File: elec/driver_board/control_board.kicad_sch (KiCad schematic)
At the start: 20 parts, among them J1 rotary_encoder, J2 DCF77 board, J3 RTC, U1 ESP32-C3-DEVKITM-1, U2 TXB0102DCT

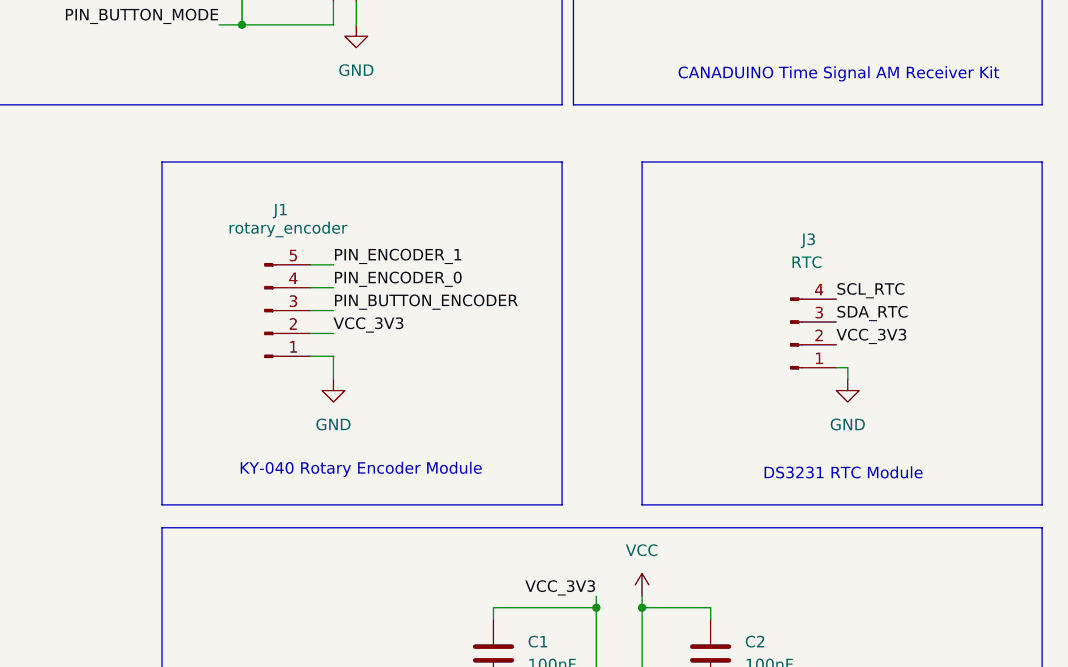
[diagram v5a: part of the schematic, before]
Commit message: Update hole size
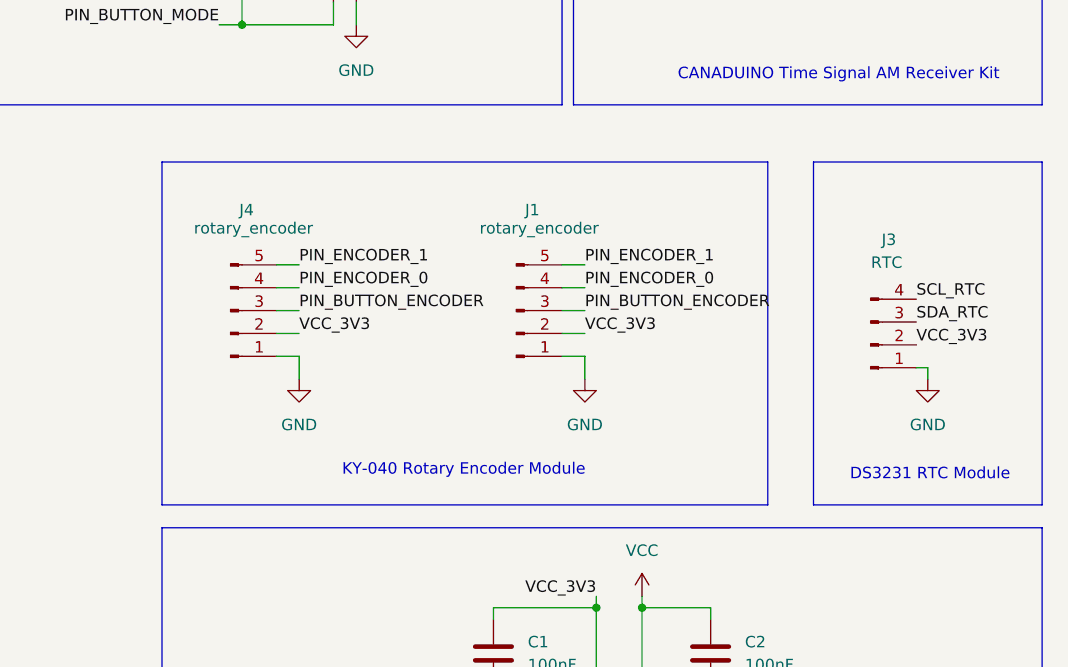
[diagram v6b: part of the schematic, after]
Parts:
- added J4: rotary_encoder, Connector_PinHeader_2.54mm:PinHeader_1x05_P2.54mm_Vertical, symbol Connector:Conn_01x05_Pin
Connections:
- net GND: now also J4.1 (Pin_1)
- net PIN_BUTTON_ENCODER: now also J4.3 (Pin_3)
- net PIN_ENCODER_0: now also J4.4 (Pin_4)
- net PIN_ENCODER_1: now also J4.5 (Pin_5)
- net VCC_3V3: now also J4.2 (Pin_2)
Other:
- moved on the sheet: J1, J3
